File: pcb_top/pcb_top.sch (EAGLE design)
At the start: 6 parts, among them X1 FH12-14S-0.5SH

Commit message: finished v1.0
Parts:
- added GND, RX, TX: TPTP20SQ, testpad:TPTP20SQ
- added JP1: (no value), pinhead:PINHD-1X4
- added R1: (no value), rcl:R-EU_R0603
- LED1: value F50360 -> (none); device led:F50360 -> led:LEDSML0805
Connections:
- new net N$1: LED1.A, R1.1
- net 3,3V: now also JP1.1
- net GND: now also GND.TP, JP1.2, LED1.C
- net LED: now also R1.2
- net RX: now also RX.TP
- net STARTER: now also JP1.3
- net TX: now also TX.TP
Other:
- note removed: "TO DO: starter LED"
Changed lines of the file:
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@@
 <part name="SV1" library="con-harting-ml" library_urn="urn:adsk.eagle:library:149" deviceset="ML10" device="" package3d_urn="urn:adsk.eagle:package:6967/1" override_package3d_urn="urn:adsk.eagle:package:39682857/2" override_package_urn="urn:adsk.eagle:footprint:6908/1"/>
 <part name="S2" library="smd-special" library_urn="urn:adsk.eagle:library:362" deviceset="SWS001" device="" package3d_urn="urn:adsk.eagle:package:26467/1" override_package3d_urn="urn:adsk.eagle:package:39682842/3" override_package_urn="urn:adsk.eagle:footprint:26408/1"/>
-<part name="LED1" library="led" library_urn="urn:adsk.eagle:library:259" deviceset="F50360" device="" package3d_urn="urn:adsk.eagle:package:15875/1"/>
+<part name="LED1" library="led" library_urn="urn:adsk.eagle:library:259" deviceset="LED" device="SML0805" package3d_urn="urn:adsk.eagle:package:15830/1"/>
 <part name="X1" library="con-hirose" library_urn="urn:adsk.eagle:library:152" deviceset="FH12-14S-0.5S" device="H" package3d_urn="urn:adsk.eagle:package:7327/1" override_package3d_urn="urn:adsk.eagle:package:39279061/2" override_package_urn="urn:adsk.eagle:footprint:7251/1"/>
 <part name="GND19" library="supply1" library_urn="urn:adsk.eagle:library:371" deviceset="GND" device=""/>
@@
 <part name="P+3" library="supply1" library_urn="urn:adsk.eagle:library:371" deviceset="VCC" device=""/>
 <part name="RN1" library="resistor-dil" library_urn="urn:adsk.eagle:library:342" deviceset="4R-N" device="CAT16" package3d_urn="urn:adsk.eagle:package:24916/1" override_package3d_urn="urn:adsk.eagle:package:35474243/2" override_package_urn="urn:adsk.eagle:footprint:24896/1"/>
+<part name="JP1" library="pinhead" library_urn="urn:adsk.eagle:library:325" deviceset="PINHD-1X4" device="" package3d_urn="urn:adsk.eagle:package:22407/2"/>
+<part name="R1" library="rcl" library_urn="urn:adsk.eagle:library:334" deviceset="R-EU_" device="R0603" package3d_urn="urn:adsk.eagle:package:23555/3"/>
+<part name="GND5" library="supply1" library_urn="urn:adsk.eagle:library:371" deviceset="GND" device=""/>
+<part name="GND6" library="supply1" library_urn="urn:adsk.eagle:library:371" deviceset="GND" device=""/>
+<part name="GND7" library="supply1" library_urn="urn:adsk.eagle:library:371" deviceset="GND" device=""/>
+<part name="P+5" library="supply1" library_urn="urn:adsk.eagle:library:371" deviceset="VCC" device=""/>
+<part name="TX" library="testpad" library_urn="urn:adsk.eagle:library:385" deviceset="TP" device="TP20SQ" package3d_urn="urn:adsk.eagle:package:27980/1"/>
+<part name="RX" library="testpad" library_urn="urn:adsk.eagle:library:385" deviceset="TP" device="TP20SQ" package3d_urn="urn:adsk.eagle:package:27980/1"/>
+<part name="GND" library="testpad" library_urn="urn:adsk.eagle:library:385" deviceset="TP" device="TP20SQ" package3d_urn="urn:adsk.eagle:package:27980/1"/>
+<part name="GND8" library="supply1" library_urn="urn:adsk.eagle:library:371" deviceset="GND" device=""/>
 </parts>
 <sheets>
 <sheet>
 <plain>
-<text x="-35.56" y="58.42" size="6.4516" layer="97">TO DO:
-starter
-LED</text>
 </plain>
 <instances>
@@
 <attribute name="NAME" x="0" y="10.16" size="1.778" layer="95" rot="R90"/>
 </instance>
-<instance part="LED1" gate="G$1" x="55.88" y="43.18" smashed="yes">
-<attribute name="NAME" x="63.5" y="43.434" size="1.778" layer="95"/>
-<attribute name="VALUE" x="63.5" y="41.275" size="1.778" layer="96"/>
+<instance part="LED1" gate="G$1" x="91.44" y="10.16" smashed="yes">
+<attribute name="NAME" x="93.98" y="10.414" size="1.778" layer="95"/>
+<attribute name="VALUE" x="99.06" y="8.255" size="1.778" layer="96"/>
 </instance>
 <instance part="X1" gate="-1" x="-33.02" y="7.62" smashed="yes" rot="MR0">
@@
 <attribute name="VALUE" x="29.718" y="48.26" size="1.778" layer="96" rot="R90"/>
 <attribute name="NAME" x="29.718" y="40.64" size="1.778" layer="95" rot="R90"/>
+</instance>
+<instance part="JP1" gate="A" x="124.46" y="15.24" smashed="yes">
+<attribute name="NAME" x="118.11" y="23.495" size="1.778" layer="95"/>
+<attribute name="VALUE" x="118.11" y="7.62" size="1.778" layer="96"/>
+</instance>
+<instance part="R1" gate="G$1" x="91.44" y="20.32" smashed="yes" rot="R90">
+<attribute name="NAME" x="89.9414" y="16.51" size="1.778" layer="95" rot="R90"/>
+<attribute name="VALUE" x="94.742" y="16.51" size="1.778" layer="96" rot="R90"/>
+</instance>
+<instance part="GND5" gate="1" x="91.44" y="0" smashed="yes">
+<attribute name="VALUE" x="88.9" y="-2.54" size="1.778" layer="96"/>
+</instance>
+<instance part="GND6" gate="1" x="91.44" y="0" smashed="yes">
+<attribute name="VALUE" x="88.9" y="-2.54" size="1.778" layer="96"/>
+</instance>
+<instance part="GND7" gate="1" x="114.3" y="0" smashed="yes">
+<attribute name="VALUE" x="111.76" y="-2.54" size="1.778" layer="96"/>
+</instance>
+<instance part="P+5" gate="VCC" x="114.3" y="30.48" smashed="yes"/>
+<instance part="TX" gate="G$1" x="-63.5" y="17.78" smashed="yes" rot="R270">
+<attribute name="NAME" x="-62.23" y="19.05" size="1.778" layer="95" rot="R270"/>
+<attribute name="TP_SIGNAL_NAME" x="-64.77" y="16.51" size="1.778" layer="97" rot="R270"/>
+</instance>
+<instance part="RX" gate="G$1" x="-63.5" y="12.7" smashed="yes" rot="R270">
+<attribute name="NAME" x="-62.23" y="13.97" size="1.778" layer="95" rot="R270"/>
+<attribute name="TP_SIGNAL_NAME" x="-64.77" y="11.43" size="1.778" layer="97" rot="R270"/>
+</instance>
+<instance part="GND" gate="G$1" x="-63.5" y="7.62" smashed="yes" rot="R270">
+<attribute name="NAME" x="-62.23" y="8.89" size="1.778" layer="95" rot="R270"/>
+<attribute name="TP_SIGNAL_NAME" x="-64.77" y="6.35" size="1.778" layer="97" rot="R270"/>
+</instance>
+<instance part="GND8" gate="1" x="-68.58" y="2.54" smashed="yes">
+<attribute name="VALUE" x="-71.12" y="0" size="1.778" layer="96"/>
 </instance>
 </instances>
@@
 <pinref part="GND3" gate="1" pin="GND"/>
 <wire x1="69.85" y1="12.7" x2="69.85" y2="2.54" width="0.1524" layer="91"/>
+</segment>
+<segment>
+<pinref part="GND5" gate="1" pin="GND"/>
+<pinref part="GND6" gate="1" pin="GND"/>
+<pinref part="LED1" gate="G$1" pin="C"/>
+<pinref part="LED1" gate="G$1" pin="C"/>
+<wire x1="91.44" y1="5.08" x2="91.44" y2="2.54" width="0.1524" layer="91"/>
+</segment>
+<segment>
+<pinref part="JP1" gate="A" pin="2"/>
+<wire x1="121.92" y1="17.78" x2="114.3" y2="17.78" width="0.1524" layer="91"/>
+<pinref part="GND7" gate="1" pin="GND"/>
+<wire x1="114.3" y1="17.78" x2="114.3" y2="2.54" width="0.1524" layer="91"/>
+</segment>
+<segment>
+<pinref part="GND" gate="G$1" pin="TP"/>
+<wire x1="-66.04" y1="7.62" x2="-68.58" y2="7.62" width="0.1524" layer="91"/>
+<pinref part="GND8" gate="1" pin="GND"/>
+<wire x1="-68.58" y1="5.08" x2="-68.58" y2="7.62" width="0.1524" layer="91"/>
 </segment>
 </net>
@@
 <pinref part="RN1" gate="A" pin="2"/>
 </segment>
+<segment>
+<pinref part="JP1" gate="A" pin="1"/>
+<wire x1="121.92" y1="20.32" x2="114.3" y2="20.32" width="0.1524" layer="91"/>
+<pinref part="P+5" gate="VCC" pin="VCC"/>
+<wire x1="114.3" y1="20.32" x2="114.3" y2="27.94" width="0.1524" layer="91"/>
+<label x="116.84" y="33.02" size="1.778" layer="95" rot="R180"/>
+</segment>
 </net>
 <net name="ROBOT_ON" class="0">
@@
 <pinref part="X1" gate="-7" pin="1"/>
 </segment>
+<segment>
+<pinref part="R1" gate="G$1" pin="2"/>
+<wire x1="91.44" y1="27.94" x2="91.44" y2="25.4" width="0.1524" layer="91"/>
+<label x="91.44" y="27.94" size="1.016" layer="95" rot="R180" xref="yes"/>
+</segment>
 </net>
 <net name="RST" class="0">
@@
 <pinref part="X1" gate="-11" pin="1"/>
 </segment>
+<segment>
+<pinref part="TX" gate="G$1" pin="TP"/>
+<wire x1="-66.04" y1="17.78" x2="-68.58" y2="17.78" width="0.1524" layer="91"/>
+<label x="-68.58" y="17.78" size="1.016" layer="95" rot="R180" xref="yes"/>
+</segment>
 </net>
 <net name="RX" class="0">
@@
 <pinref part="X1" gate="-12" pin="1"/>
 </segment>
+<segment>
+<pinref part="RX" gate="G$1" pin="TP"/>
+<wire x1="-66.04" y1="12.7" x2="-68.58" y2="12.7" width="0.1524" layer="91"/>
+<label x="-68.58" y="12.7" size="1.016" layer="95" rot="R180" xref="yes"/>
+</segment>
 </net>
 <net name="STARTER" class="0">
@@
 <wire x1="-25.4" y1="38.1" x2="-30.48" y2="38.1" width="0.1524" layer="91"/>
 <pinref part="X1" gate="-13" pin="1"/>
+</segment>
+<segment>
+<pinref part="JP1" gate="A" pin="3"/>
+<wire x1="121.92" y1="15.24" x2="111.76" y2="15.24" width="0.1524" layer="91"/>
+<label x="111.76" y="15.24" size="1.016" layer="95" rot="R180" xref="yes"/>
 </segment>
 </net>
@@
 <wire x1="36.83" y1="7.62" x2="36.83" y2="17.78" width="0.1524" layer="91"/>
 <label x="43.18" y="22.86" size="1.778" layer="95" rot="R180"/>
+</segment>
+</net>
+<net name="N$1" class="0">
+<segment>
+<pinref part="LED1" gate="G$1" pin="A"/>
+<pinref part="R1" gate="G$1" pin="1"/>
+<wire x1="91.44" y1="12.7" x2="91.44" y2="15.24" width="0.1524" layer="91"/>
 </segment>
 </net>
@@
 </drawing>
 <compatibility>
-<note version="6.3" minversion="6.2.2" severity="warning">
-Since Version 6.2.2 text objects can contain more than one line,
-which will not be processed correctly with this version.
-</note>
 <note version="8.2" severity="warning">
 Since Version 8.2, EAGLE supports online libraries. The ids
@@
 will not be understood (or retained) with this version.
 </note>
+<note version="8.4" severity="warning">
+Since Version 8.4, EAGLE supports properties for SPICE simulation.
+Probes in schematics and SPICE mapping objects found in parts and library devices
+will not be understood with this version. Update EAGLE to the latest version
+for full support of SPICE simulation.
+</note>
 </compatibility>

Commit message: minor changes
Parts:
- LED1: device led:LEDSML0805 -> led:LEDCHIP-LED0805
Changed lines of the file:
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@@
 <part name="SV1" library="con-harting-ml" library_urn="urn:adsk.eagle:library:149" deviceset="ML10" device="" package3d_urn="urn:adsk.eagle:package:6967/1" override_package3d_urn="urn:adsk.eagle:package:39682857/2" override_package_urn="urn:adsk.eagle:footprint:6908/1"/>
 <part name="S2" library="smd-special" library_urn="urn:adsk.eagle:library:362" deviceset="SWS001" device="" package3d_urn="urn:adsk.eagle:package:26467/1" override_package3d_urn="urn:adsk.eagle:package:39682842/3" override_package_urn="urn:adsk.eagle:footprint:26408/1"/>
-<part name="LED1" library="led" library_urn="urn:adsk.eagle:library:259" deviceset="LED" device="SML0805" package3d_urn="urn:adsk.eagle:package:15830/1"/>
+<part name="LED1" library="led" library_urn="urn:adsk.eagle:library:259" deviceset="LED" device="CHIP-LED0805" package3d_urn="urn:adsk.eagle:package:15818/2"/>
 <part name="X1" library="con-hirose" library_urn="urn:adsk.eagle:library:152" deviceset="FH12-14S-0.5S" device="H" package3d_urn="urn:adsk.eagle:package:7327/1" override_package3d_urn="urn:adsk.eagle:package:39279061/2" override_package_urn="urn:adsk.eagle:footprint:7251/1"/>
 <part name="GND19" library="supply1" library_urn="urn:adsk.eagle:library:371" deviceset="GND" device=""/>
@@
 <pinref part="GND6" gate="1" pin="GND"/>
 <pinref part="LED1" gate="G$1" pin="C"/>
-<pinref part="LED1" gate="G$1" pin="C"/>
 <wire x1="91.44" y1="5.08" x2="91.44" y2="2.54" width="0.1524" layer="91"/>

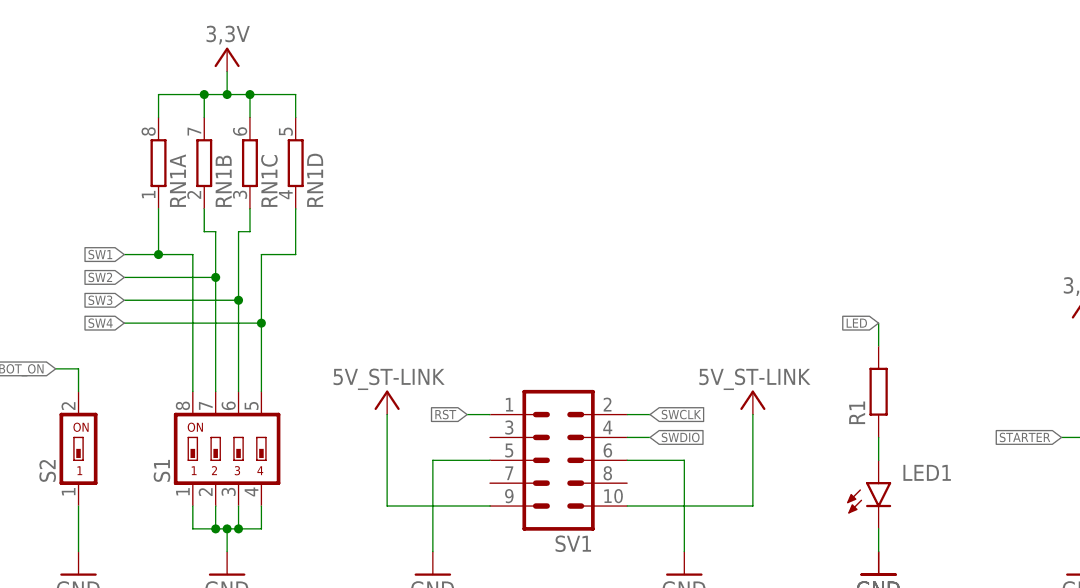
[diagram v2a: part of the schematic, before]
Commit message: adjust component values
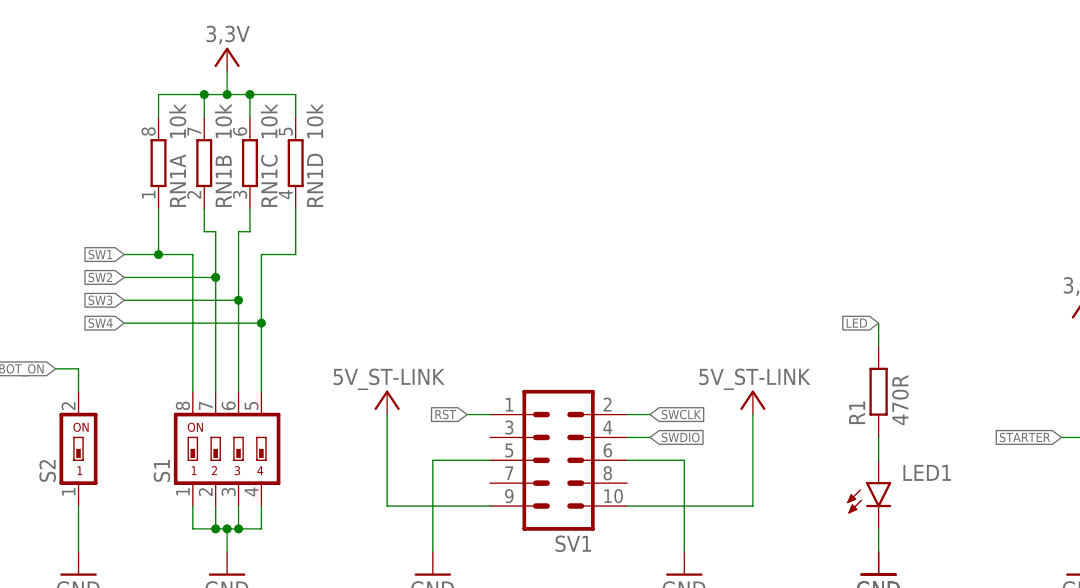
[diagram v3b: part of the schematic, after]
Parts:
- R1: value (none) -> 470R
- RN1: value (none) -> 10k
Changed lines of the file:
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@@
 <part name="P+2" library="supply1" library_urn="urn:adsk.eagle:library:371" deviceset="VCC" device=""/>
 <part name="P+3" library="supply1" library_urn="urn:adsk.eagle:library:371" deviceset="VCC" device=""/>
-<part name="RN1" library="resistor-dil" library_urn="urn:adsk.eagle:library:342" deviceset="4R-N" device="CAT16" package3d_urn="urn:adsk.eagle:package:24916/1" override_package3d_urn="urn:adsk.eagle:package:35474243/2" override_package_urn="urn:adsk.eagle:footprint:24896/1"/>
+<part name="RN1" library="resistor-dil" library_urn="urn:adsk.eagle:library:342" deviceset="4R-N" device="CAT16" package3d_urn="urn:adsk.eagle:package:24916/1" override_package3d_urn="urn:adsk.eagle:package:35474243/2" override_package_urn="urn:adsk.eagle:footprint:24896/1" value="10k"/>
 <part name="JP1" library="pinhead" library_urn="urn:adsk.eagle:library:325" deviceset="PINHD-1X4" device="" package3d_urn="urn:adsk.eagle:package:22407/2"/>
-<part name="R1" library="rcl" library_urn="urn:adsk.eagle:library:334" deviceset="R-EU_" device="R0603" package3d_urn="urn:adsk.eagle:package:23555/3"/>
+<part name="R1" library="rcl" library_urn="urn:adsk.eagle:library:334" deviceset="R-EU_" device="R0603" package3d_urn="urn:adsk.eagle:package:23555/3" value="470R"/>
 <part name="GND5" library="supply1" library_urn="urn:adsk.eagle:library:371" deviceset="GND" device=""/>
 <part name="GND6" library="supply1" library_urn="urn:adsk.eagle:library:371" deviceset="GND" device=""/>
